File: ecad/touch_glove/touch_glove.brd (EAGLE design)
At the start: 78.3 x 40.6 mm, 177 parts, among them Q1 MCH3474 4A/30V, Q2 MCH3474 4A/30V, Q3 MCH3474 4A/30V, Q4 MCH3474 4A/30V, Q5 MCH3474 4A/30V, Q6 MCH3474 4A/30V, SW1 4A/28V

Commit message: Update libraries.
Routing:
- net NGND: vias 90 -> 86
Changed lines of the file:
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@@
 <wire x1="48.85" y1="31.45" x2="48.6" y2="31.7" width="0.254" layer="1"/>
 <wire x1="19.575" y1="12.425" x2="19.575" y2="10.6" width="0.508" layer="1"/>
-<via x="15.7" y="5.7" extent="1-16" drill="0.254"/>
-<via x="14.9" y="5.7" extent="1-16" drill="0.254"/>
-<via x="13.8" y="6.7" extent="1-16" drill="0.254"/>
-<via x="13.8" y="5.8" extent="1-16" drill="0.254"/>
 </signal>
 <signal name="3.3V">

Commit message: Add several test codes for PCB.
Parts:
- LIPO1: value Molex RA 2mm pitch -> 7.4V
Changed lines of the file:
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@@
 <?xml version="1.0" encoding="utf-8"?>
 <!DOCTYPE eagle SYSTEM "eagle.dtd">
-<eagle version="9.1.0">
+<eagle version="9.1.3">
 <drawing>
 <settings>
@@
 <attribute name="MFR" value="Comchip Technology" x="31.9" y="13" size="1.778" layer="27" rot="R270" display="off"/>
 <attribute name="MPN" value="CGRKM4001-HF" x="31.9" y="13" size="1.778" layer="27" rot="R270" display="off"/>
+<attribute name="VALUE" value="1A/50V" x="31.9" y="13" size="1.778" layer="27" rot="R270" display="off"/>
 </element>
 <element name="D3" library="PiB_discrete_semiconductors" package="SODFL3516X170" package3d_urn="urn:adsk.eagle:package:2939213/1" value="1A/50V" x="20" y="19.8" rot="R270">
@@
 <attribute name="MFR" value="Comchip Technology" x="20" y="19.8" size="1.778" layer="27" rot="R270" display="off"/>
 <attribute name="MPN" value="CGRKM4001-HF" x="20" y="19.8" size="1.778" layer="27" rot="R270" display="off"/>
+<attribute name="VALUE" value="1A/50V" x="20" y="19.8" size="1.778" layer="27" rot="R270" display="off"/>
 </element>
 <element name="D6" library="PiB_discrete_semiconductors" package="DFN100X60X55-2" package3d_urn="urn:adsk.eagle:package:2933421/1" value="150mA/75V" x="45.9" y="34.2" rot="R180">
@@
 <attribute name="VALUE" value="250mA/3.3V" x="46.9" y="12.5" size="1.778" layer="27" rot="R90" display="off"/>
 </element>
-<element name="LIPO1" library="PiB_batteries" package="BATTERY_MOLEX-89401_RA_PITCH-2MM" package3d_urn="urn:adsk.eagle:package:2971487/3" value="Molex RA 2mm pitch" x="19.2" y="6.7" rot="R180">
+<element name="LIPO1" library="PiB_batteries" package="BATTERY_MOLEX-89401_RA_PITCH-2MM" package3d_urn="urn:adsk.eagle:package:2971487/3" value="7.4V" x="19.2" y="6.7" rot="R180">
 <attribute name="DATASHEET" value="https://www.molex.com/pdm_docs/sd/894010210_sd.pdf" x="19.2" y="6.7" size="1.778" layer="27" font="vector" rot="R180" display="off"/>
 <attribute name="DATASHEET_CONNECTOR" value="https://www.molex.com/pdm_docs/sd/873690200_sd.pdf" x="19.2" y="6.7" size="1.778" layer="27" font="vector" rot="R180" display="off"/>

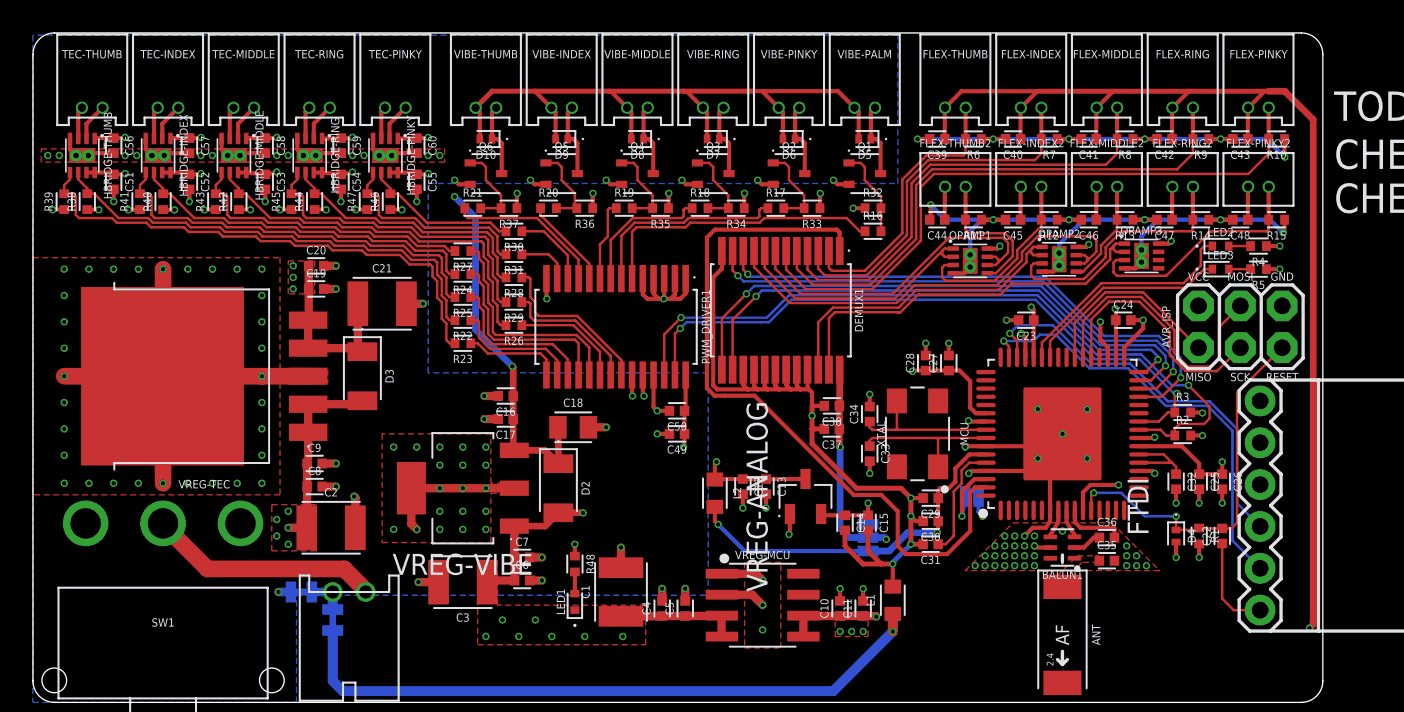
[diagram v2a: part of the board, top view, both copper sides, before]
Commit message: Massive updates to code.  Changed touch glove PCB to Rev 3 with 1.8V regulator, confirmed to work.
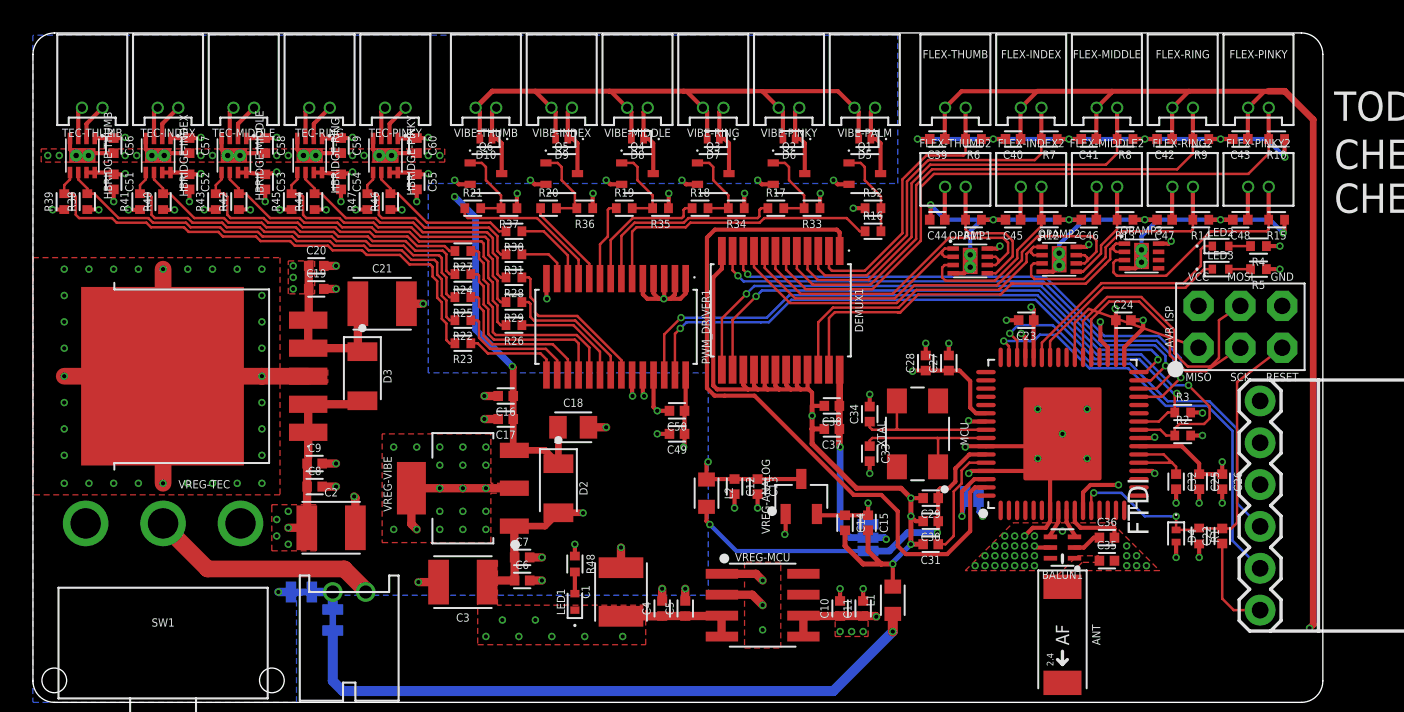
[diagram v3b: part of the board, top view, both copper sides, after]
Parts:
- AVR_ISP: value AVRISP -> PTH VERT MALE; device PiB_connectors:2X3-NS -> PiB_connectors:HDRV6W64P254_2X3_762X483X838B_AVR-ISP
- L1, L2: device PiB_inductors:INDC1608X60 -> PiB_inductors:INDC1608X60-0603
- VREG-ANALOG: value 250mA/3.3V -> MCP1700-1802 1.8V/200mA
- moved AVR_ISP 2.84 mm to (70.8, 21.5)
- moved C12 0.51 mm to (42.6, 13.1)
- moved C13 0.51 mm to (44.0, 13.1)
- moved L2 0.51 mm to (40.9, 12.7)
- moved VREG-ANALOG 0.25 mm to (46.6, 12.5)
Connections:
- net N$39 renamed AREF
- net NGND: now also VREG-VIBE.TAB; no longer VREG-VIBE.4
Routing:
- net MISO: track 11.8 -> 10.4 mm
- net AVCC: track 22.4 -> 22.9 mm
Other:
- board text added: "Touch Glove Rev 3"
- board text removed: "Touch Glove Rev 2"

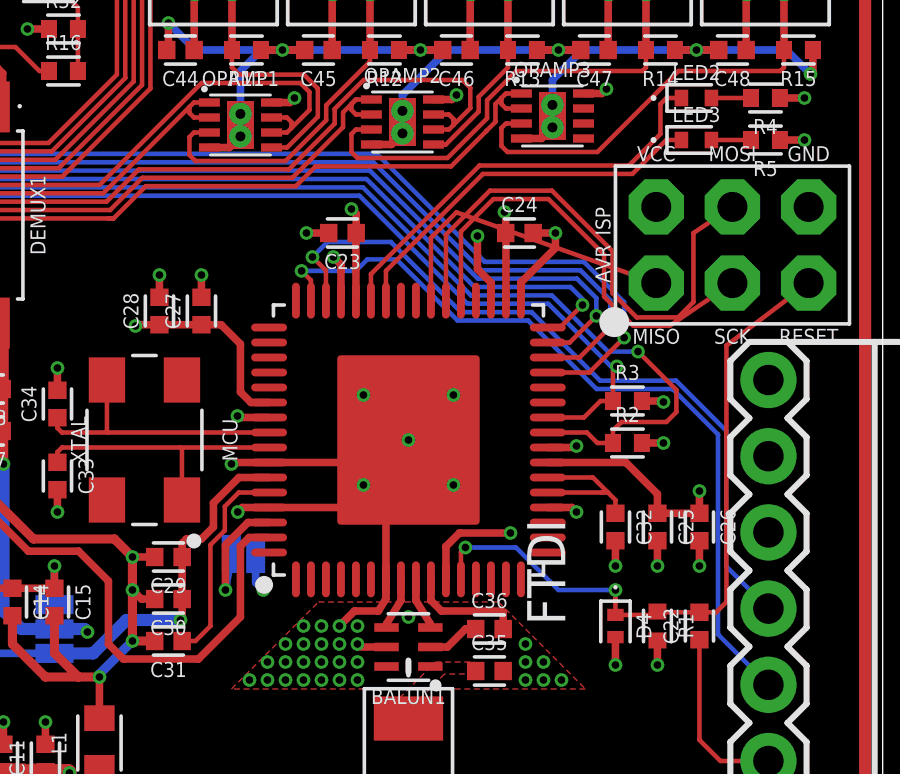
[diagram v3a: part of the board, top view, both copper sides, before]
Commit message: Start on Rev 2 of robotic arm.  Made minor fixes to Touch Glove Rev 2.
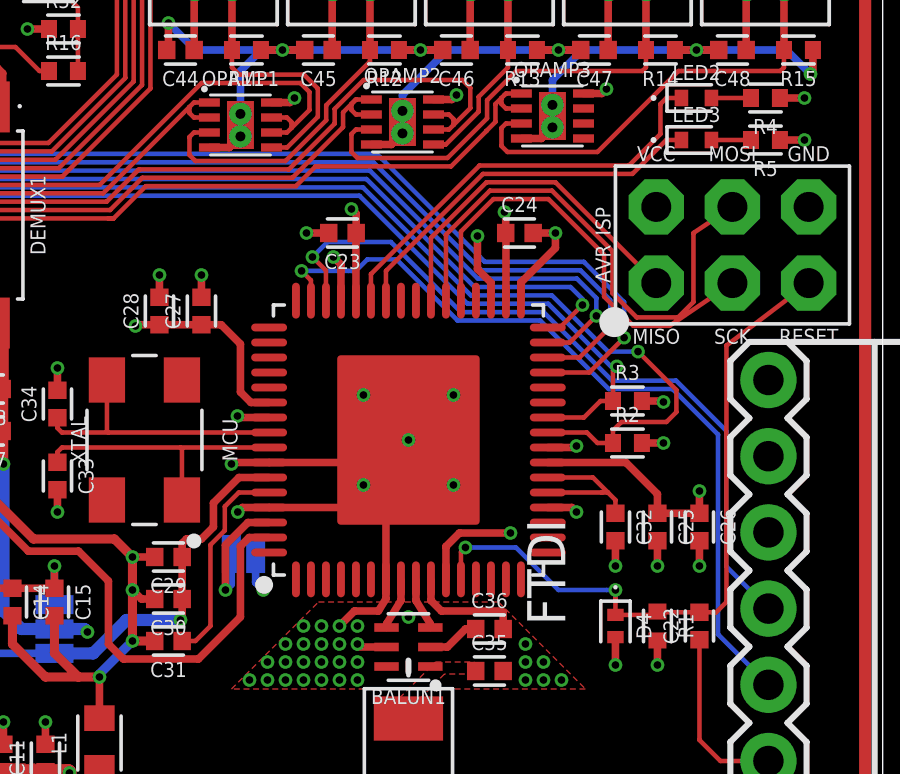
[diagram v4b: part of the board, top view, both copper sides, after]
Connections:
- net N$33 renamed A1.8V
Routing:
- net MISO: track 10.4 -> 11.8 mm

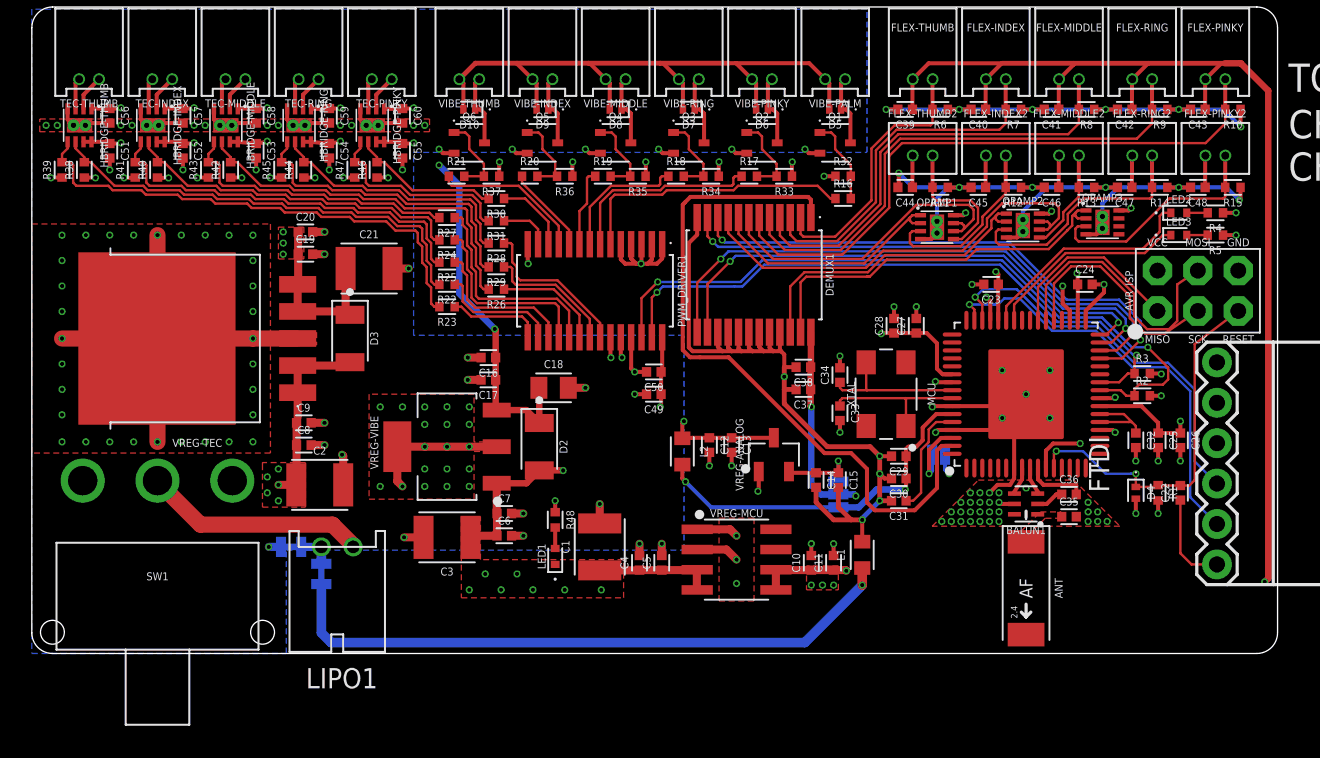
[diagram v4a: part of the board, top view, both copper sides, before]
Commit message: Rev 3: Changes to robotic and and touch glove to fix inconsistencies and errors from Rev 2.
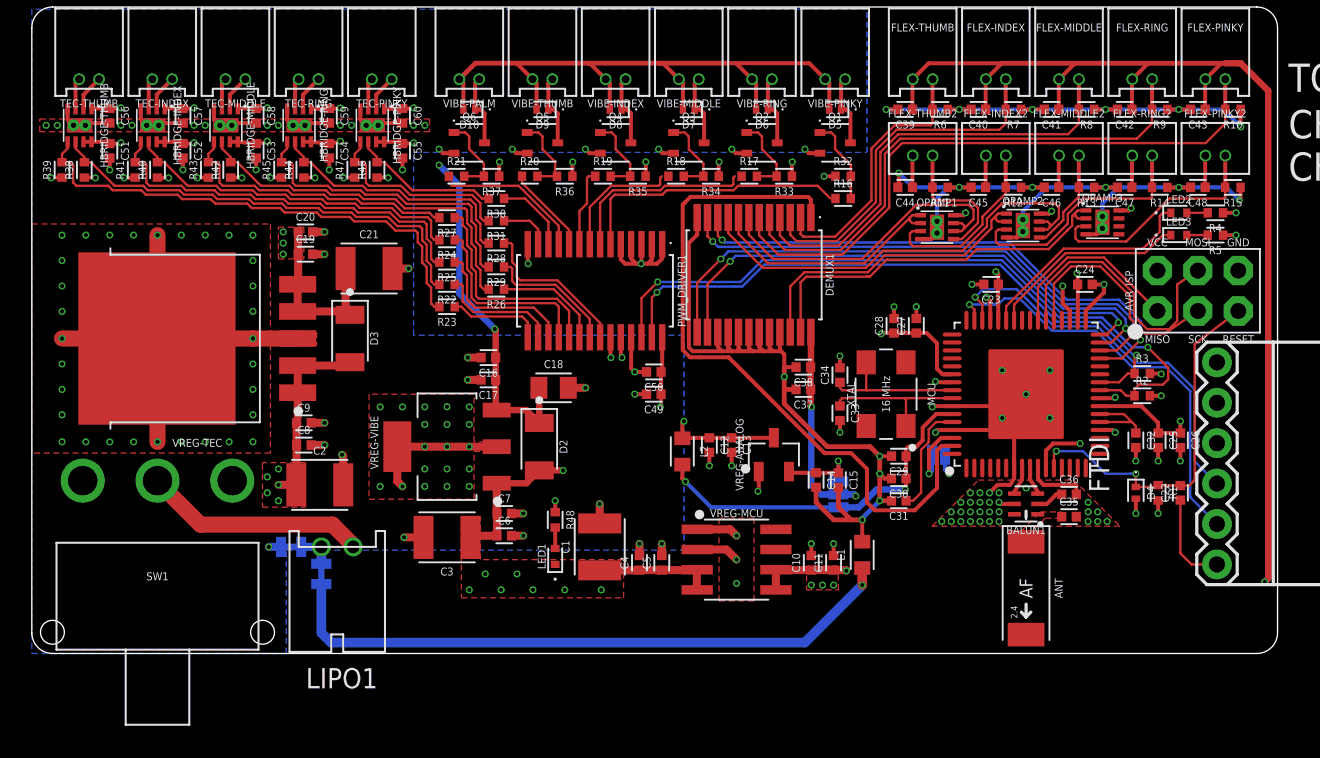
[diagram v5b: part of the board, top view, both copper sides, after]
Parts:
- moved VIBE-PALM 23.0 mm to (27.5, 36.1)
- moved VIBE-INDEX 4.60 mm to (36.7, 36.1)
- moved VIBE-PINKY 4.60 mm to (50.5, 36.1)
- moved VIBE-RING 4.60 mm to (45.9, 36.1)
- moved VIBE-THUMB 4.60 mm to (32.1, 36.1)
- moved VIBE-MIDDLE 4.60 mm to (41.3, 36.1)
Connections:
- net N$15: now also VIBE-RING.2; no longer VIBE-PINKY.2
- net N$17: now also VIBE-PINKY.2; no longer VIBE-PALM.2
- net N$2: now also VIBE-INDEX.2; no longer VIBE-MIDDLE.2
- net N$3: now also VIBE-THUMB.2; no longer VIBE-INDEX.2
- net N$30: now also VIBE-PALM.2; no longer VIBE-THUMB.2
- net N$4: now also VIBE-MIDDLE.2; no longer VIBE-RING.2
- net NGND: now also VREG-TEC.TAB; no longer VREG-TEC.6
- net VIBE-INDEX: now also PWM_DRIVER1.9, R19.1; no longer PWM_DRIVER1.10, R20.1
- net VIBE-MIDDLE: now also PWM_DRIVER1.8, R18.1; no longer PWM_DRIVER1.9, R19.1
- net VIBE-PALM: now also PWM_DRIVER1.11, R21.1; no longer PWM_DRIVER1.6, R16.1
- net VIBE-PINKY: now also PWM_DRIVER1.6, R16.1; no longer PWM_DRIVER1.7, R17.1
- net VIBE-RING: now also PWM_DRIVER1.7, R17.1; no longer PWM_DRIVER1.8, R18.1
- net VIBE-THUMB: now also PWM_DRIVER1.10, R20.1; no longer PWM_DRIVER1.11, R21.1
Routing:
- net VIBE-PALM: track 17.7 -> 9.18 mm
- net VIBE-PINKY: track 12.4 -> 17.3 mm
- net VIBE-THUMB: track 9.60 -> 5.50 mm
- net VIBE-RING: track 8.32 -> 12.0 mm
- net VIBE-MIDDLE: track 4.93 -> 7.90 mm
- net VIBE-INDEX: track 5.50 -> 4.93 mm
